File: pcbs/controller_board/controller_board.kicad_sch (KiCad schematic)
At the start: 33 parts, among them J1 RJ45, J2 PINHD-1X7, J3 PINHD-1X12, J4 PINHD-1X4, P1 24V / 5A, Q1 220mA / 50V, Q2 220mA / 50V, U1 8-28V in / 5V 5W out, U2 Particle2 / Boron, U3 A: 1.2 to 3.3V B: 1.8 to 5.5V

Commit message: update part info
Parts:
- C1: JLCPCB (none) -> C1884; JLCPCBURL (none) -> https://jlcpcb.com/partdetail/2236-1206CG101J500NT/C1884
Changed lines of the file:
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@@
+			)
+		)
+		(property "JLCPCB" "C1884"
+			(at 104.14 119.38 90)
+			(effects
+				(font
+					(size 1.27 1.27)
+				)
+				(hide yes)
+			)
+		)
+		(property "JLCPCBURL" "https://jlcpcb.com/partdetail/2236-1206CG101J500NT/C1884"
+			(at 104.14 119.38 90)
+			(effects
+				(font
+					(size 1.27 1.27)
+				)
+				(hide yes)
 			)
 		)

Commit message: update controller board to version 1.1 - i2c level shifting back to mosfets
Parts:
- removed C1: 100pF, footprints:C_1206, symbol symbols:C
- removed R15: 200kΩ, footprints:R_1206, symbol symbols:R_US
- removed U3: A: 1.2 to 3.3V B: 1.8 to 5.5V, footprints:SOT-765-1_VSSOP8, symbol symbols:LevelShifter_PCA9306
- added Q3, Q4: 220mA / 50V, footprints:SOT-23-3, symbol symbols:Q_NMOS_220mA_50V
- R11: value 2.2kΩ -> 10kΩ; JLCPCB C17948 -> (none); JLCPCBURL https://jlcpcb.com/partdetail/18636-1206W4F2201T5E/C17948 -> (none)
- R12, R13, R14: value 2.2kΩ -> 10kΩ
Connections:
- net +3V3: now also R14.2, Q3.1 (G), Q4.1 (G); no longer R11.2
- net +5V: no longer R13.2, R14.2
- net 5V-SCL: now also R11.2, Q3.3 (D); no longer R13.1
- net 5V-SDA: now also R13.2, Q4.3 (D); no longer R14.1
- net D0-SDA: now also R14.1, Q4.2 (S); no longer R11.1
- net D1-SCL: now also Q3.2 (S)
- net Vout renamed +5Vout
- net +5Vout: now also R11.1, R13.1

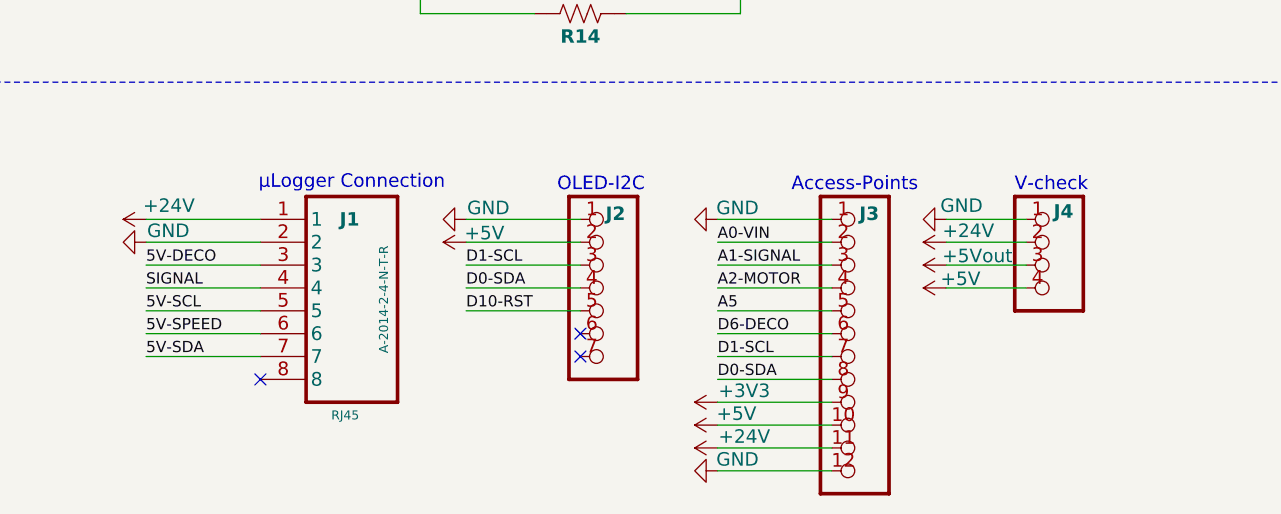
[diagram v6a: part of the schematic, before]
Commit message: use updated header symbols, otherwise no changes
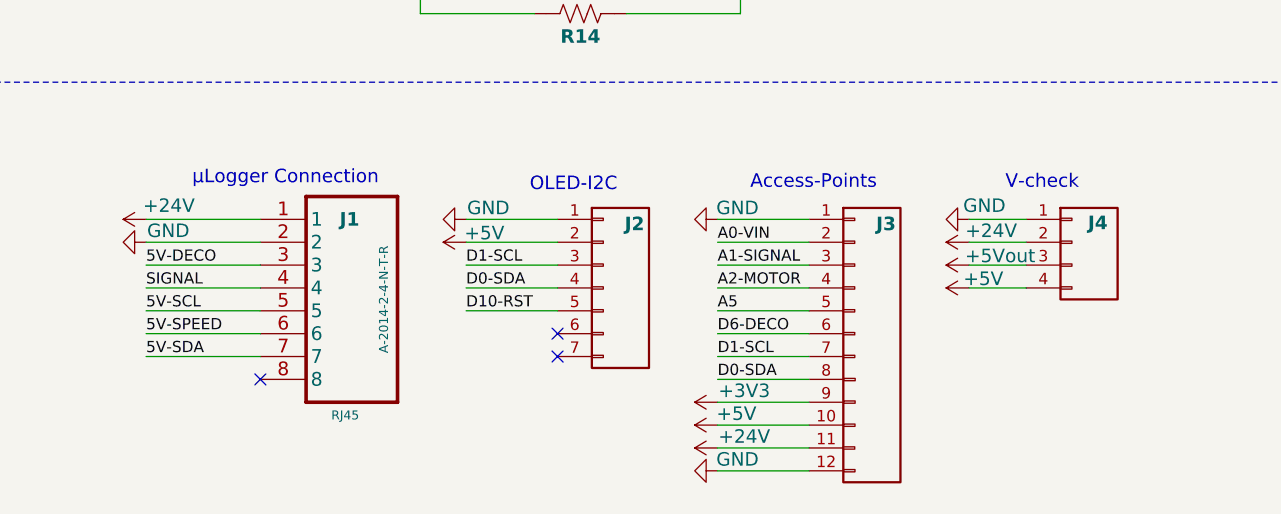
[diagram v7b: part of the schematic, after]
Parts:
- J2: value PINHD-1X7 -> Conn_01x07
- J3: value PINHD-1X12 -> Conn_01x12

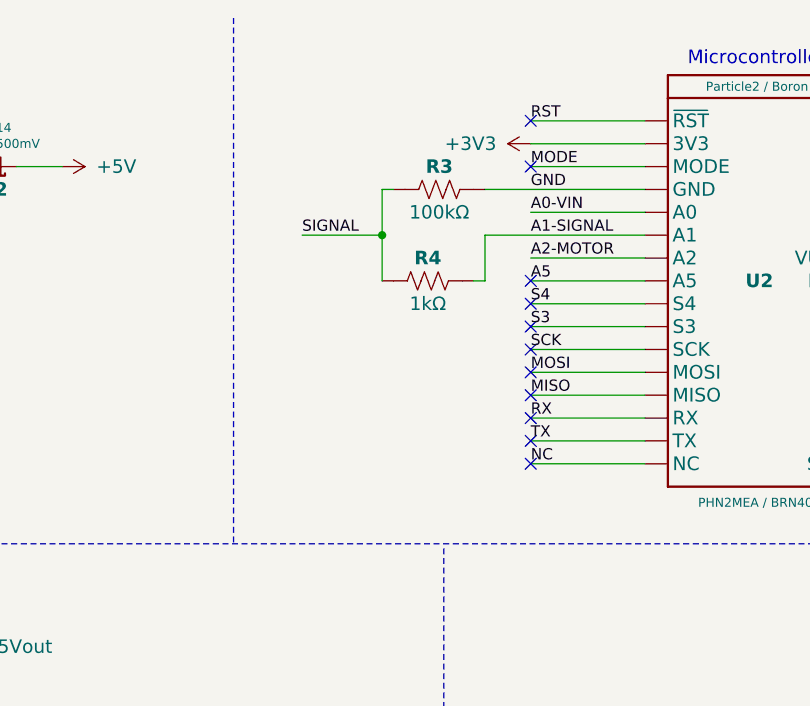
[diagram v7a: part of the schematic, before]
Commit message: add signal stabilizing capacitors to controller and sensor boards
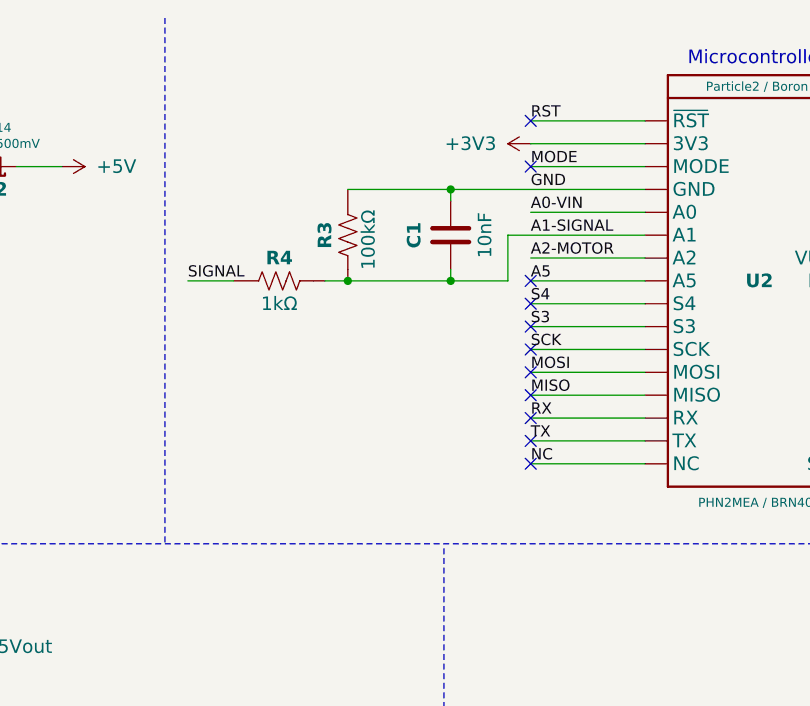
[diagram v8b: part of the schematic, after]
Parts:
- added C1: 10nF, footprints:C_0603, symbol symbols:C_0603
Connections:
- net A1-SIGNAL: now also R3.1, C1.1
- net GND: now also C1.2
- net SIGNAL: no longer R3.1
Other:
- moved on the sheet: R3, R4
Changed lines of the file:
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@@
 	)
 	(junction
-		(at 170.18 36.83)
-		(diameter 0)
-		(color 0 0 0 0)
-	)
-	(junction
 		(at 60.96 29.21)
 		(diameter 0)
@@
 	)
 	(junction
+		(at 177.8 41.91)
+		(diameter 0)
+		(color 0 0 0 0)
+	)
+	(junction
 		(at 74.93 123.19)
 		(diameter 0)
@@
 	)
 	(junction
+		(at 177.8 31.75)
+		(diameter 0)
+		(color 0 0 0 0)
+	)
+	(junction
 		(at 109.22 59.69)
 		(diameter 0)
@@
 	)
 	(junction
+		(at 166.37 41.91)
+		(diameter 0)
+		(color 0 0 0 0)
+	)
+	(junction
 		(at 246.38 137.16)
 		(diameter 0)
@@
 	(wire
 		(pts
+			(xy 177.8 41.91) (xy 184.15 41.91)
+		)
+		(stroke
+			(width 0.1524)
+			(type solid)
+		)
+	)
+	(wire
+		(pts
 			(xy 110.49 93.98) (xy 120.65 93.98)
 		)
@@
 	(wire
 		(pts
-			(xy 170.18 36.83) (xy 161.29 36.83)
+			(xy 148.59 41.91) (xy 153.67 41.91)
 		)
 		(stroke
@@
 	(wire
 		(pts
+			(xy 177.8 40.64) (xy 177.8 41.91)
+		)
+		(stroke
+			(width 0)
+			(type default)
+		)
+	)
+	(wire
+		(pts
 			(xy 110.49 91.44) (xy 110.49 82.55)
 		)
@@
 	(wire
 		(pts
+			(xy 163.83 41.91) (xy 166.37 41.91)
+		)
+		(stroke
+			(width 0)
+			(type default)
+		)
+	)
+	(wire
+		(pts
 			(xy 118.11 177.8) (xy 107.95 177.8)
 		)
@@
 	(wire
 		(pts
-			(xy 181.61 41.91) (xy 181.61 36.83)
+			(xy 184.15 41.91) (xy 184.15 36.83)
 		)
 		(stroke
@@
 	(wire
 		(pts
-			(xy 170.18 31.75) (xy 170.18 36.83)
-		)
-		(stroke
-			(width 0)
-			(type default)
-		)
-	)
-	(wire
-		(pts
 			(xy 118.11 185.42) (xy 107.95 185.42)
 		)
@@
 	(wire
 		(pts
-			(xy 181.61 31.75) (xy 199.39 31.75)
-		)
-		(stroke
-			(width 0)
-			(type default)
-		)
-	)
-	(wire
-		(pts
-			(xy 170.18 41.91) (xy 170.18 36.83)
-		)
-		(stroke
-			(width 0)
-			(type default)
-		)
-	)
-	(wire
-		(pts
 			(xy 87.63 139.7) (xy 74.93 139.7)
 		)
@@
 		)
 	)
-	(wire
-		(pts
-			(xy 171.45 31.75) (xy 170.18 31.75)
-		)
-		(stroke
-			(width 0)
-			(type default)
-		)
-	)
 	(polyline
 		(pts
@@
 	(wire
 		(pts
+			(xy 177.8 31.75) (xy 199.39 31.75)
+		)
+		(stroke
+			(width 0)
+			(type default)
+		)
+	)
+	(wire
+		(pts
 			(xy 224.79 62.23) (xy 240.03 62.23)
 		)
@@
 	(polyline
 		(pts
-			(xy 153.67 12.7) (xy 153.67 71.12)
+			(xy 146.05 12.7) (xy 146.05 71.12)
 		)
 		(stroke
@@
 	(wire
 		(pts
+			(xy 177.8 31.75) (xy 177.8 33.02)
+		)
+		(stroke
+			(width 0)
+			(type default)
+		)
+	)
+	(wire
+		(pts
 			(xy 118.11 187.96) (xy 107.95 187.96)
 		)
@@
 	(wire
 		(pts
+			(xy 166.37 31.75) (xy 177.8 31.75)
+		)
+		(stroke
+			(width 0)
+			(type default)
+		)
+	)
+	(wire
+		(pts
 			(xy 118.11 172.72) (xy 107.95 172.72)
 		)
@@
 	(wire
 		(pts
+			(xy 166.37 41.91) (xy 177.8 41.91)
+		)
+		(stroke
+			(width 0)
+			(type default)
+		)
+	)
+	(wire
+		(pts
 			(xy 30.48 29.21) (xy 36.83 29.21)
 		)
@@
 	(wire
 		(pts
-			(xy 181.61 36.83) (xy 199.39 36.83)
+			(xy 184.15 36.83) (xy 199.39 36.83)
 		)
 		(stroke
@@
 		)
 	)
-	(wire
-		(pts
-			(xy 181.61 41.91) (xy 180.34 41.91)
-		)
-		(stroke
-			(width 0.1524)
-			(type solid)
-		)
-	)
 	(image
 		(at 276.86 173.99)
@@
 	)
 	(label "SIGNAL"
-		(at 161.29 36.83 0)
+		(at 148.59 41.91 0)
 		(effects
 			(font
@@
 	(symbol
 		(lib_id "symbols:R_US")
-		(at 175.26 41.91 180)
+		(at 158.75 41.91 180)
 		(unit 1)
 		(exclude_from_sim no)
@@
 		(dnp no)
 		(property "Reference" "R4"
-			(at 175.26 39.37 0)
+			(at 158.75 39.37 0)
 			(effects
 				(font
@@
 		)
 		(property "Value" "1kΩ"
-			(at 175.26 44.45 0)
+			(at 158.75 44.45 0)
 			(effects
 				(font
@@
 		)
 		(property "Footprint" "footprints:R_1206"
-			(at 174.244 41.656 90)
+			(at 157.734 41.656 90)
 			(effects
 				(font
@@
 		)
 		(property "Datasheet" "~"
-			(at 175.26 41.91 0)
+			(at 158.75 41.91 0)
 			(effects
 				(font
@@
 		)
 		(property "Description" "Resistor, US symbol"
-			(at 175.26 41.91 0)
+			(at 158.75 41.91 0)
 			(effects
 				(font
@@
 	)
 	(symbol
+		(lib_id "symbols:C_0603")
+		(at 177.8 36.83 270)
+		(unit 1)
+		(exclude_from_sim no)
+		(in_bom yes)
+		(on_board yes)
+		(dnp no)
+		(fields_autoplaced yes)
+		(property "Reference" "C1"
+			(at 173.736 36.83 0)
+			(do_not_autoplace yes)
+			(effects
+				(font
+					(size 1.5 1.5)
+					(thickness 0.254)
+					(bold yes)
+				)
+			)
+		)
+		(property "Value" "10nF"
+			(at 181.61 36.83 0)
+			(do_not_autoplace yes)
+			(effects
+				(font
+					(size 1.5 1.5)
+				)
+			)
+		)
+		(property "Footprint" "footprints:C_0603"
+			(at 173.99 37.7952 0)
+			(effects
+				(font
+					(size 1.27 1.27)
+				)
+				(hide yes)
+			)
+		)
+		(property "Datasheet" "~"
+			(at 177.8 36.83 0)
+			(effects
+				(font
+					(size 1.27 1.27)
+				)
+				(hide yes)
+			)
+		)
+		(property "Description" "Unpolarized capacitor"
+			(at 177.8 36.83 0)
+			(effects
+				(font
+					(size 1.27 1.27)
+				)
+				(hide yes)
+			)
+		)
+		(property "JLCPCB" "C1589"
+			(at 177.8 36.83 0)
+			(effects
+				(font
+					(size 1.27 1.27)
+				)
+				(hide yes)
+			)
+		)
+		(property "JLCPCBURL" "https://jlcpcb.com/partdetail/1941-CL10B103KB8NNNC/C1589"
+			(at 177.8 36.83 0)
+			(effects
+				(font
+					(size 1.27 1.27)
+				)
+				(hide yes)
+			)
+		)
+		(pin "1"
+		)
+		(pin "2"
+		)
+		(instances
+			(project ""
+				(path "/ba44af6b-d897-4c95-8815-b8860eb38091"
+					(reference "C1")
+					(unit 1)
+				)
+			)
+		)
+	)
+	(symbol
 		(lib_id "symbols:+3V3")
 		(at 203.2 137.16 90)
@@
 	(symbol
 		(lib_id "symbols:R_US")
-		(at 176.53 31.75 180)
+		(at 166.37 36.83 270)
 		(unit 1)
 		(exclude_from_sim no)
@@
 		(dnp no)
 		(property "Reference" "R3"
-			(at 176.53 29.21 0)
+			(at 163.83 36.83 0)
 			(effects
 				(font
@@
 		)
 		(property "Value" "100kΩ"
-			(at 176.53 34.29 0)
+			(at 168.656 37.338 0)
 			(effects
 				(font
@@
 		)
 		(property "Footprint" "footprints:R_1206"
-			(at 175.514 31.496 90)
+			(at 166.116 37.846 90)
 			(effects
 				(font
@@
 		)
 		(property "Datasheet" "~"
-			(at 176.53 31.75 0)
+			(at 166.37 36.83 0)
 			(effects
 				(font
@@
 		)
 		(property "Description" "Resistor, US symbol"
-			(at 176.53 31.75 0)
+			(at 166.37 36.83 0)
 			(effects
 				(font
@@
 		)
 		(property "JLCPCB" "C17900"
-			(at 176.53 31.75 0)
+			(at 166.37 36.83 0)
 			(effects
 				(font
@@
 		)
 		(property "JLCPCBURL" "https://jlcpcb.com/partdetail/18588-1206W4F1003T5E/C17900"
-			(at 176.53 31.75 0)
+			(at 166.37 36.83 0)
 			(effects
 				(font
